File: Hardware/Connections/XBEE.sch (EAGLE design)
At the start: 4 parts

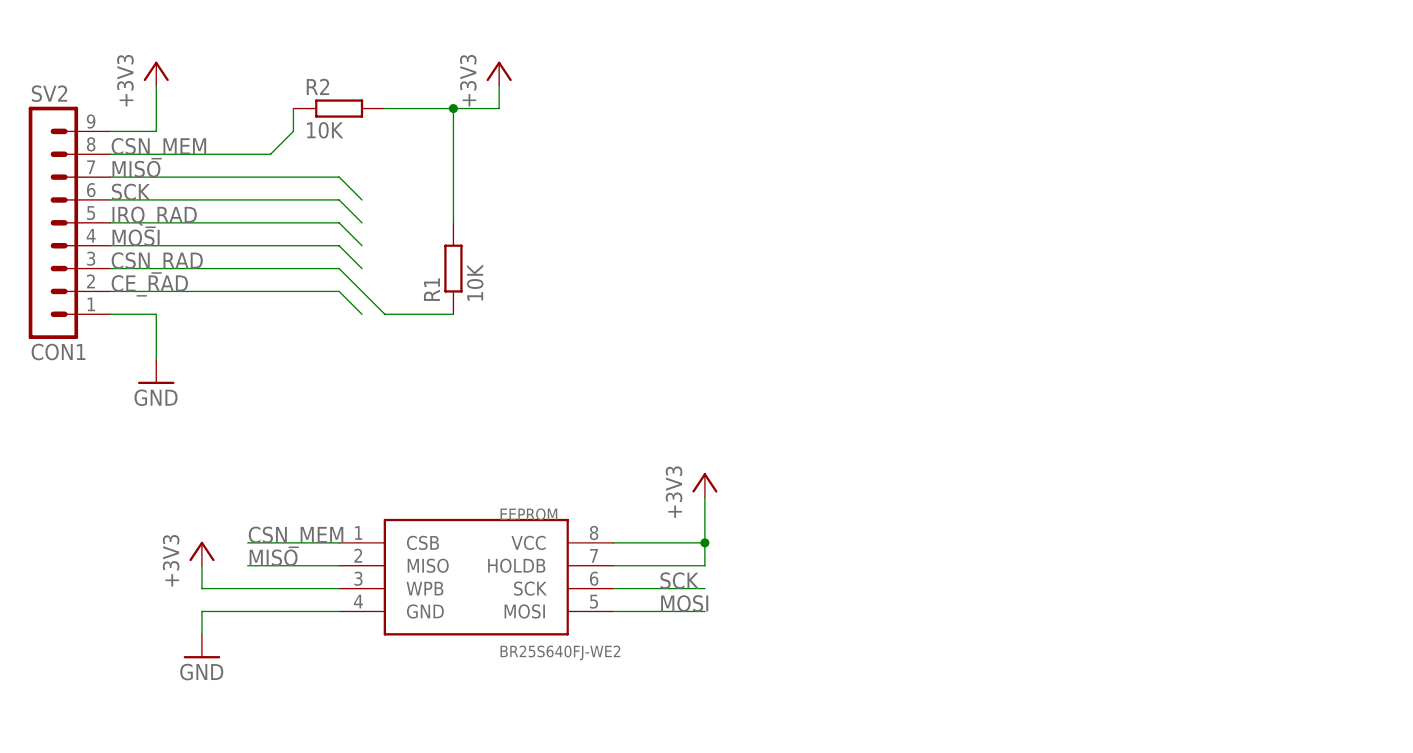
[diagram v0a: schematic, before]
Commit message: updated XBEE Schematic. Added 3 Extra Pins for Serial protocol
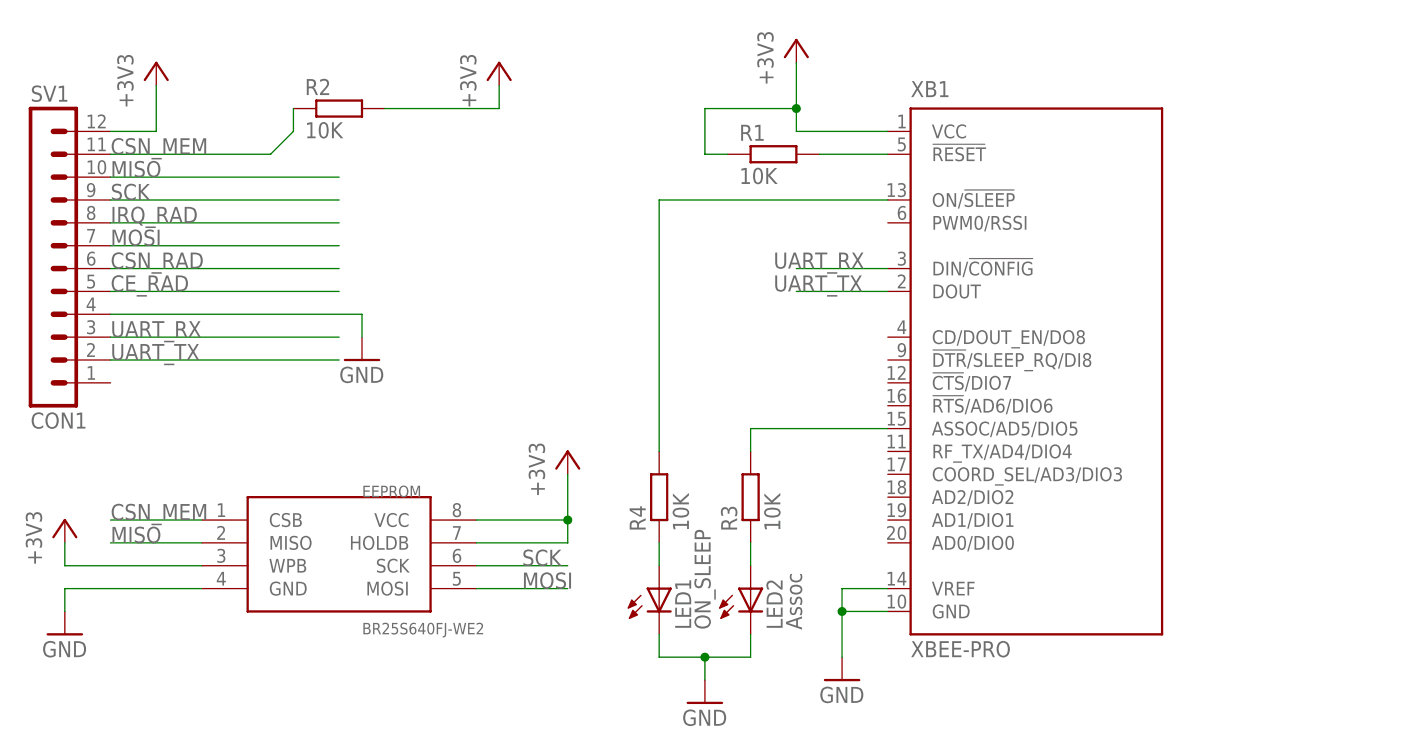
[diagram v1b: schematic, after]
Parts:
- removed SV2: CON1, con-lstb:MA09-1W
- added LED1: ON_SLEEP, led:LEDSMT1206
- added LED2: Assoc, led:LEDSMT1206
- added R3, R4: 10K, resistor:R-EU_R1206
- added SV1: CON1, con-lstb:MA12-1W
- added XB1: XBEE-PRO, maxstream:XBEE-PRO
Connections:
- new net N$1: R1.2, XB1.!RESET
- new net N$3: R4.2, XB1.ON/!SLEEP
- new net N$5: R3.2, XB1.ASSOC/AD5/DIO5
- new net N$6: LED1.A, R4.1
- new net N$7: LED2.A, R3.1
- new net UART_RX: SV1.3, XB1.DIN/!CONFIG
- new net UART_TX: SV1.2, XB1.DOUT
- net +3V3: now also R1.1, SV1.12, XB1.VCC; no longer R1.2, SV2.9
- net CE_RAD: now also SV1.5; no longer SV2.2
- net CSN_MEM: now also SV1.11; no longer SV2.8
- net CSN_RAD: now also SV1.6; no longer R1.1, SV2.3
- net GND: now also LED1.C, LED2.C, SV1.4, XB1.GND, XB1.VREF; no longer SV2.1
- net IRQ_RAD: now also SV1.8; no longer SV2.5
- net MISO: now also SV1.10; no longer SV2.7
- net MOSI: now also SV1.7; no longer SV2.4
- net SCK: now also SV1.9; no longer SV2.6
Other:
- moved on the sheet: EEPROM, R1

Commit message: added missing components to XBEE schematic
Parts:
- added C1: 8.2p, rcl:C-EUC1206
- added C2: 1u, rcl:C-EUC1206
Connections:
- net +3V3: now also C1.1, C2.1
- net GND: now also C1.2, C2.2
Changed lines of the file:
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@@
 <part name="LED1" library="led" deviceset="LED" device="SMT1206" value="ON_SLEEP"/>
 <part name="LED2" library="led" deviceset="LED" device="SMT1206" value="Assoc"/>
+<part name="+3V5" library="supply1" deviceset="+3V3" device=""/>
+<part name="GND5" library="supply1" deviceset="GND" device=""/>
+<part name="C1" library="rcl" deviceset="C-EU" device="C1206" value="8.2p"/>
+<part name="C2" library="rcl" deviceset="C-EU" device="C1206" value="1u"/>
 </parts>
 <sheets>
@@
 <instance part="LED1" gate="G$1" x="60.96" y="12.7"/>
 <instance part="LED2" gate="G$1" x="71.12" y="12.7"/>
+<instance part="+3V5" gate="G$1" x="132.08" y="73.66"/>
+<instance part="GND5" gate="1" x="132.08" y="53.34"/>
+<instance part="C1" gate="G$1" x="124.46" y="63.5"/>
+<instance part="C2" gate="G$1" x="137.16" y="63.5"/>
 </instances>
 <busses>
@@
 <junction x="76.2" y="66.04"/>
 </segment>
+<segment>
+<pinref part="+3V5" gate="G$1" pin="+3V3"/>
+<wire x1="132.08" y1="71.12" x2="132.08" y2="68.58" width="0.1524" layer="91"/>
+<pinref part="C2" gate="G$1" pin="1"/>
+<wire x1="132.08" y1="68.58" x2="137.16" y2="68.58" width="0.1524" layer="91"/>
+<wire x1="137.16" y1="68.58" x2="137.16" y2="66.04" width="0.1524" layer="91"/>
+<pinref part="C1" gate="G$1" pin="1"/>
+<wire x1="132.08" y1="68.58" x2="124.46" y2="68.58" width="0.1524" layer="91"/>
+<wire x1="124.46" y1="68.58" x2="124.46" y2="66.04" width="0.1524" layer="91"/>
+<junction x="132.08" y="68.58"/>
+</segment>
 </net>
 <net name="GND" class="0">
@@
 <junction x="66.04" y="5.08"/>
 </segment>
+<segment>
+<pinref part="C1" gate="G$1" pin="2"/>
+<pinref part="GND5" gate="1" pin="GND"/>
+<wire x1="124.46" y1="58.42" x2="132.08" y2="58.42" width="0.1524" layer="91"/>
+<wire x1="132.08" y1="58.42" x2="132.08" y2="55.88" width="0.1524" layer="91"/>
+<pinref part="C2" gate="G$1" pin="2"/>
+<wire x1="137.16" y1="58.42" x2="132.08" y2="58.42" width="0.1524" layer="91"/>
+<junction x="132.08" y="58.42"/>
+</segment>
 </net>
